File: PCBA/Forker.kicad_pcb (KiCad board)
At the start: 2 copper layers, 60.5 x 51 mm, 48 parts, among them J1 USB C, J11 Conn_01x05, J12 Conn_02x06_Odd_Even, J2 Conn_01x02, J3 Conn_01x06, J4 AA, J5 AA, J6 Conn_01x02, J7 Conn_01x02, J8 Conn_01x02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

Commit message: Update PCB Layout
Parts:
- removed J2, J9: Conn_01x02, Connector_PinHeader_2.54mm:PinHeader_1x02_P2.54mm_Vertical
- removed the R12 at (120.9, 66.0)
- removed U8: HL118, Local_Footprints:SOP-8-1EP_3.9x4.9mm_P1.27mm_EP2.4x3.3mm
- added JP2: SolderJumper_2_Open, Jumper:SolderJumper-2_P1.3mm_Open_TrianglePad1.0x1.5mm, B.Cu at (121.6, 82.9)
- added JP3: SolderJumper_2_Open, Jumper:SolderJumper-2_P1.3mm_Open_TrianglePad1.0x1.5mm, B.Cu at (118.8, 82.9)
- added JP4: SolderJumper_2_Open, Jumper:SolderJumper-2_P1.3mm_Open_TrianglePad1.0x1.5mm, B.Cu at (127.4, 83.0)
- C8, J1, J11, J12, L2, SW8: moved to B.Cu
- moved D5 66.3 mm to (110.5, 67.0), turned to 180 degrees
- moved R5 64.3 mm to (116.5, 66.7), turned to 90 degrees
- moved R12 63.6 mm to (118.1, 66.7), turned to 90 degrees
- moved L2 61.0 mm to (113.3, 72.3), turned to 90 degrees
- moved C8 60.7 mm to (113.2, 79.5), turned to 180 degrees
- moved U1 36.7 mm to (104.5, 65.5), turned to -90 degrees
- moved J1 36.0 mm to (103.7, 77.3), turned to 90 degrees
- moved D3 31.2 mm to (134.5, 51.0), turned to -90 degrees
- moved U4 30.6 mm to (117.5, 71.1)
- moved U2 29.9 mm to (114.2, 62.3)
- moved D2 28.1 mm to (132.9, 51.0), turned to -90 degrees
- moved C6 27.8 mm to (114.2, 58.8), turned to 0 degrees
- moved JP1 27.1 mm to (109.5, 63.3), turned to -90 degrees
- moved J12 26.8 mm to (154.5, 71.7), turned to 180 degrees
- moved C2 24.3 mm to (108.6, 59.4)
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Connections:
- R4 pad 1: unconnected-(R4-Pad1) -> GND
- R4 pad 2: unconnected-(R4-Pad2) -> Net-(U1-TS)
- U1 pad 1: unconnected-(U1-TS-Pad1) -> Net-(U1-TS)
- U3 pad 8: Net-(U3-PA2/ROSC) -> unconnected-(U3-PA2/ROSC-Pad8)
- U5 pad 1: (no net) -> unconnected-(U5-NC-Pad1)
- U5 pad 9: (no net) -> Net-(JP2-A)
- U6 pad 1: (no net) -> unconnected-(U6-NC-Pad1)
- U6 pad 3: Net-(U3-PA18/A7/BSL) -> Net-(U3-PA17)
- U6 pad 9: (no net) -> Net-(JP3-A)
- U7 pad 1: (no net) -> unconnected-(U7-NC-Pad1)
- U7 pad 2: Net-(U3-PA17) -> Net-(U3-PA6)
- U7 pad 3: Net-(U3-PA6) -> Net-(U3-PA4)
- U7 pad 9: (no net) -> Net-(JP4-A)
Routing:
- net GND: track 0.00 -> 300.6 mm, vias 0 -> 15
- net Net-(D5-K): track 0.00 -> 69.1 mm, vias 0 -> 3
- net +5V: track 0.00 -> 65.8 mm, vias 0 -> 1
- net Net-(U2-EN): track 0.00 -> 54.2 mm, vias 0 -> 2
- net /RADIO_TX: track 0.00 -> 52.6 mm
- net /RADIO_RX: track 0.00 -> 51.2 mm
- net Net-(J12-Pin_1): track 0.00 -> 43.0 mm, vias 0 -> 2
- net /RADIO_BOOT: track 0.00 -> 41.8 mm, vias 0 -> 2
- net +BATT: track 0.00 -> 39.0 mm, vias 0 -> 3
- net +3V3: track 0.00 -> 36.8 mm, vias 0 -> 4
- net Net-(U3-PA17): track 0.00 -> 34.4 mm, vias 0 -> 2
- net Net-(U3-PA24/A3): track 0.00 -> 27.9 mm, vias 0 -> 2
- net Net-(U3-PA6): track 0.00 -> 21.2 mm
- net Net-(U3-PA4): track 0.00 -> 20.8 mm
- net Net-(U3-PA27/A0): track 0.00 -> 20.4 mm
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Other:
- board size 60.5 x 51 mm -> 60.5 x 40 mm

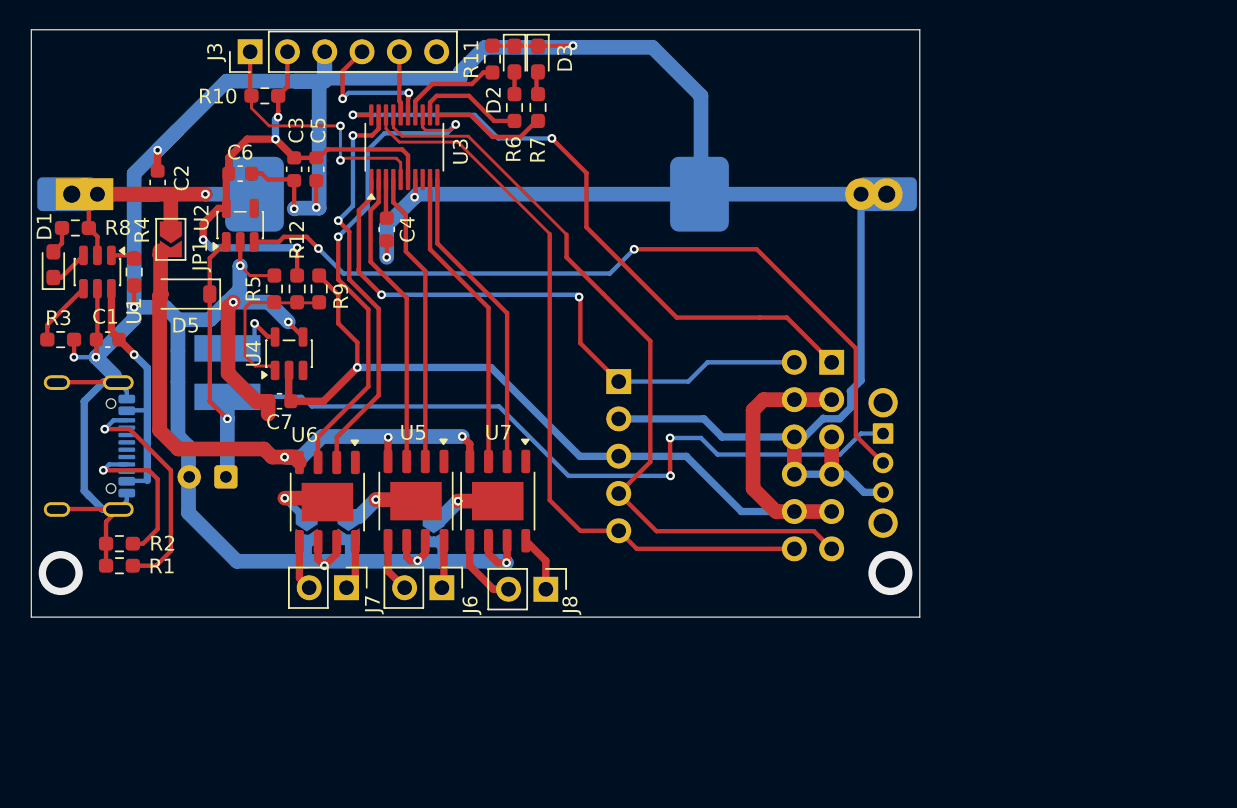
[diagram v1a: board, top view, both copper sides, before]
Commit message: -Update PCBA connector location -Add cutouts for PCBA -Add Mounting Holes
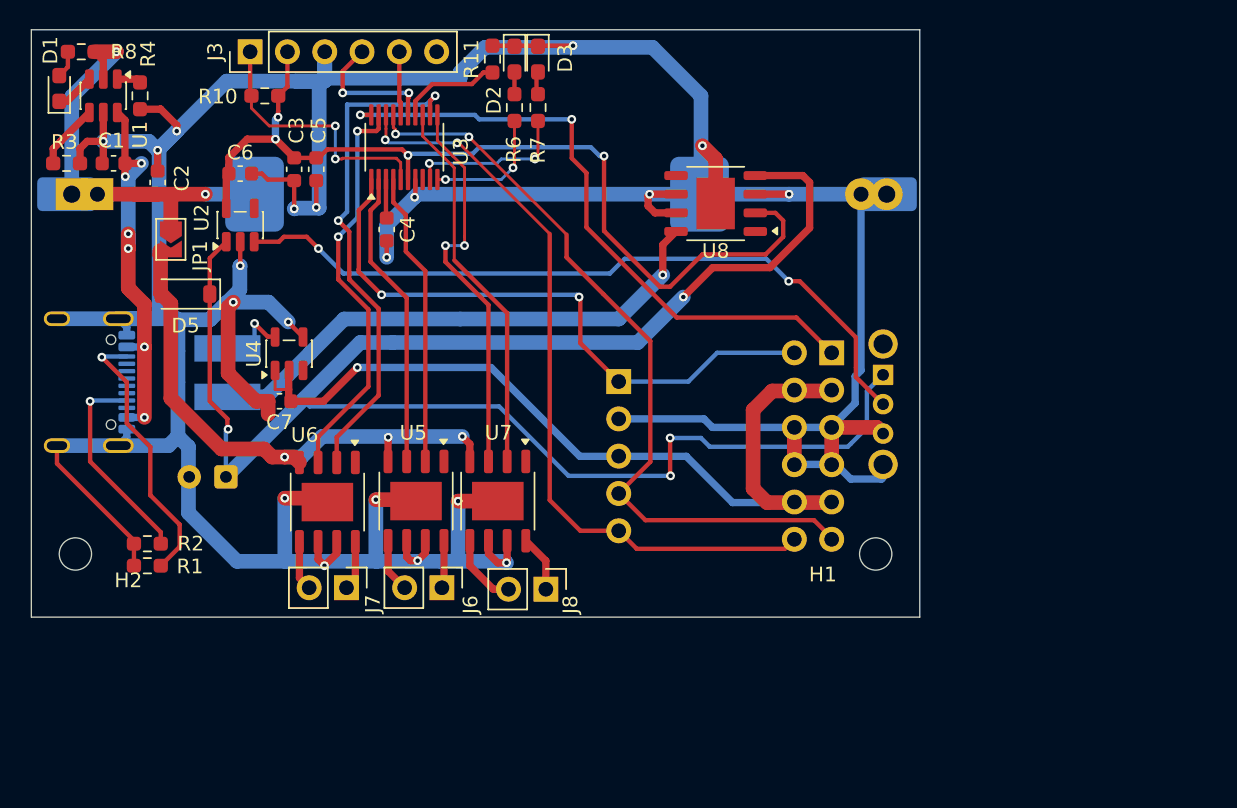
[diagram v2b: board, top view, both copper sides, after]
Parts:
- removed JP2, JP3, JP4: SolderJumper_2_Open, Jumper:SolderJumper-2_P1.3mm_Open_TrianglePad1.0x1.5mm
- removed R12, R5, R9: 10k, Resistor_SMD:R_0603_1608Metric_Pad0.98x0.95mm_HandSolder
- added H1: MountingHole, MountingHole:MountingHole_2.2mm_M2, F.Cu at (157.5, 84.7)
- added H2: MountingHole, MountingHole:MountingHole_2.2mm_M2, F.Cu at (103.0, 84.7)
- added U8: HL118, Local_Footprints:SOP-8-1EP_3.9x4.9mm_P1.27mm_EP2.4x3.3mm, F.Cu at (146.6, 60.8)
- moved D1 12.0 mm to (101.9, 53.0)
- moved R4 12.0 mm to (107.4, 53.5)
- moved R8 12.0 mm to (103.4, 50.5)
- moved U1 12.0 mm to (104.9, 53.5)
- moved C1 12.0 mm to (105.6, 58.1)
- moved R3 12.0 mm to (102.4, 58.1)
- moved J1 4.35 mm to (103.7, 73.0)
- moved SW8 4.00 mm to (158.0, 74.5)
- moved R1 1.90 mm to (107.9, 85.5)
- moved R2 1.90 mm to (107.9, 84.0)
- moved J12 0.65 mm to (154.5, 71.0)
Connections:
- L2 pad 1: Net-(D5-K) -> Net-(U8-VOUTA)
- R6 pad 1: Net-(U3-PA16/A8) -> Net-(U3-PA6)
- R7 pad 1: Net-(U3-PA11) -> Net-(U3-PA4)
- U4 pad 1: Net-(U4-CE) -> +5V
- U5 pad 9: Net-(JP2-A) -> GND
- U6 pad 2: Net-(U3-PA24/A3) -> Net-(U3-PA16/A8)
- U6 pad 3: Net-(U3-PA17) -> Net-(U3-PA24/A3)
- U6 pad 9: Net-(JP3-A) -> GND
- U7 pad 2: Net-(U3-PA6) -> Net-(U3-PA17)
- U7 pad 3: Net-(U3-PA4) -> Net-(U3-PA11)
- U7 pad 9: Net-(JP4-A) -> GND
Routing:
- net Net-(D5-K): track 69.1 -> 118.8 mm, vias 3 -> 4
- net Net-(U8-VOUTA): track 0.00 -> 36.4 mm, vias 0 -> 1
- net GND: track 300.6 -> 328.8 mm, vias 15 -> 20
- net Net-(U3-PA16/A8): track 7.50 -> 34.6 mm, vias 0 -> 2
- net +3V3: track 36.8 -> 62.5 mm
- net Net-(U3-PA11): track 7.82 -> 26.9 mm, vias 0 -> 2
- net Net-(U3-PA6): track 21.2 -> 8.71 mm, vias 0 -> 2
- net Net-(U4-CE): track 10.9 -> 0.00 mm
- net Net-(BT1-+): track 19.9 -> 30.7 mm, vias 1 -> 2
- net Net-(U1-VIN): track 17.3 -> 27.3 mm, vias 1 -> 6
- net Net-(U3-PA4): track 20.8 -> 11.1 mm, vias 0 -> 2
- net Net-(U3-PA17): track 34.4 -> 26.0 mm, vias 2 -> 0
- net +5V: track 65.8 -> 60.4 mm
- net Net-(JP2-A): track 5.11 -> 0.00 mm, vias 1 -> 0
- net Net-(JP3-A): track 5.03 -> 0.00 mm, vias 1 -> 0
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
